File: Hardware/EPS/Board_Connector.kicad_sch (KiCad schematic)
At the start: 6 parts, among them J601 Conn_02x20_Odd_Even, U601 PESD3V3L4BHCYL, U602 PESD3V3L4BHCYL, U603 PESD3V3L4BHCYL

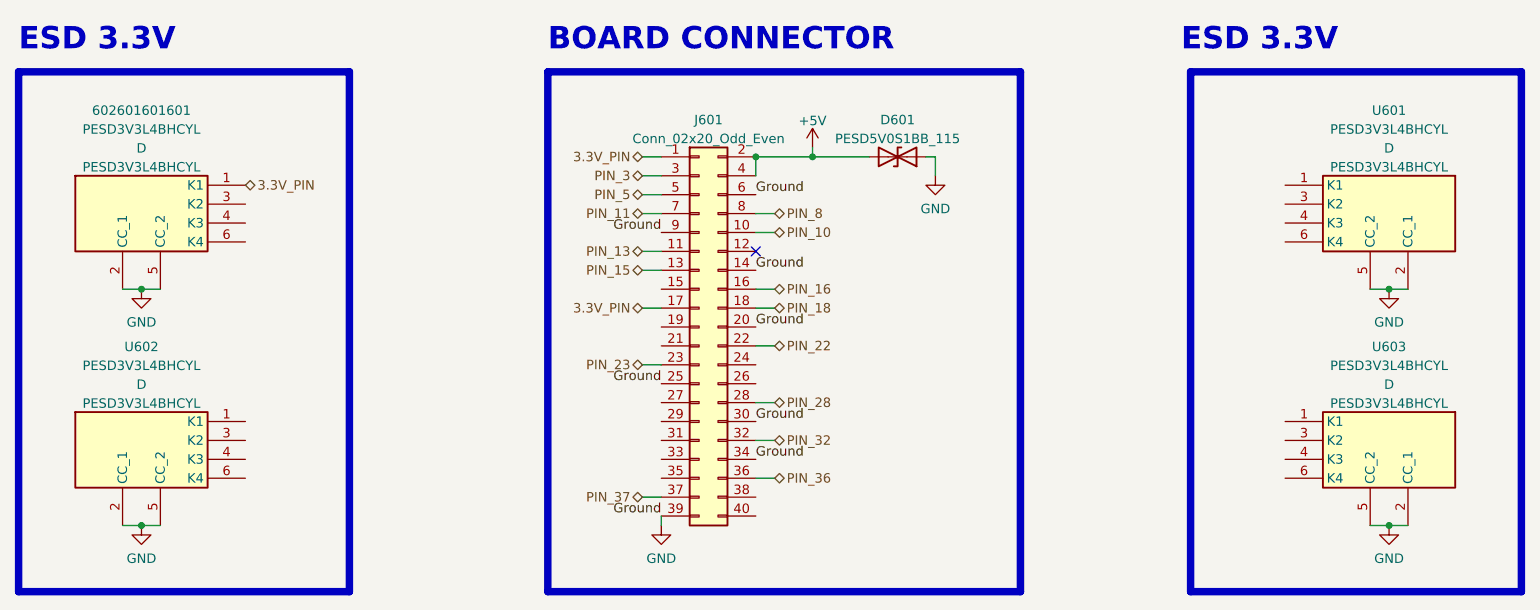
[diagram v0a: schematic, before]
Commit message: Changed uC pinout and finished uC routing
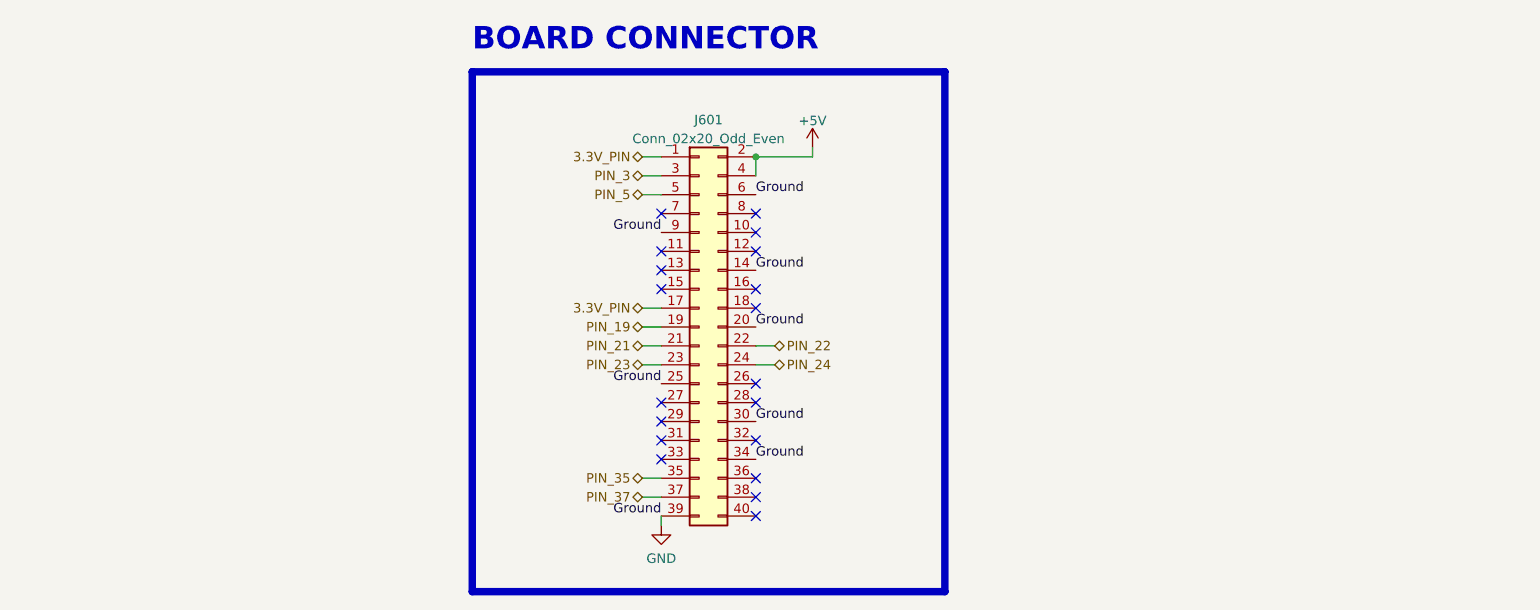
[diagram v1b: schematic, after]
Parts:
- removed 602601601601, U601, U602, U603: PESD3V3L4BHCYL, PESD3V3L4BHCYL:SON45P80X130X43-6N, symbol PESD3V3L4BHCYL:PESD3V3L4BHCYL
- removed D601: PESD5V0S1BB_115, Diode_SMD:D_SOD-523, symbol Device:D_TVS
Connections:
- net PIN_19: now reaches J601.19 (Pin_19)
- net PIN_21: now reaches J601.21 (Pin_21)
- net PIN_24: now reaches J601.24 (Pin_24)
- net PIN_35: now reaches J601.35 (Pin_35)
- net PIN_10: no longer names the net of J601.10 (Pin_10)
- net PIN_11: no longer names the net of J601.7 (Pin_7)
- net PIN_13: no longer names the net of J601.11 (Pin_11)
- net PIN_15: no longer names the net of J601.13 (Pin_13)
- net PIN_16: no longer names the net of J601.16 (Pin_16)
- net PIN_18: no longer names the net of J601.18 (Pin_18)
- net PIN_28: no longer names the net of J601.28 (Pin_28)
- net PIN_32: no longer names the net of J601.32 (Pin_32)
- net PIN_36: no longer names the net of J601.36 (Pin_36)
- net PIN_8: no longer names the net of J601.8 (Pin_8)
- no-connect marks 1 -> 19
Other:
- note removed: "ESD 3.3V"
